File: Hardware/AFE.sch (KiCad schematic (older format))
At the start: 38 parts, among them U801 4069, U802 MCP47CXBX2

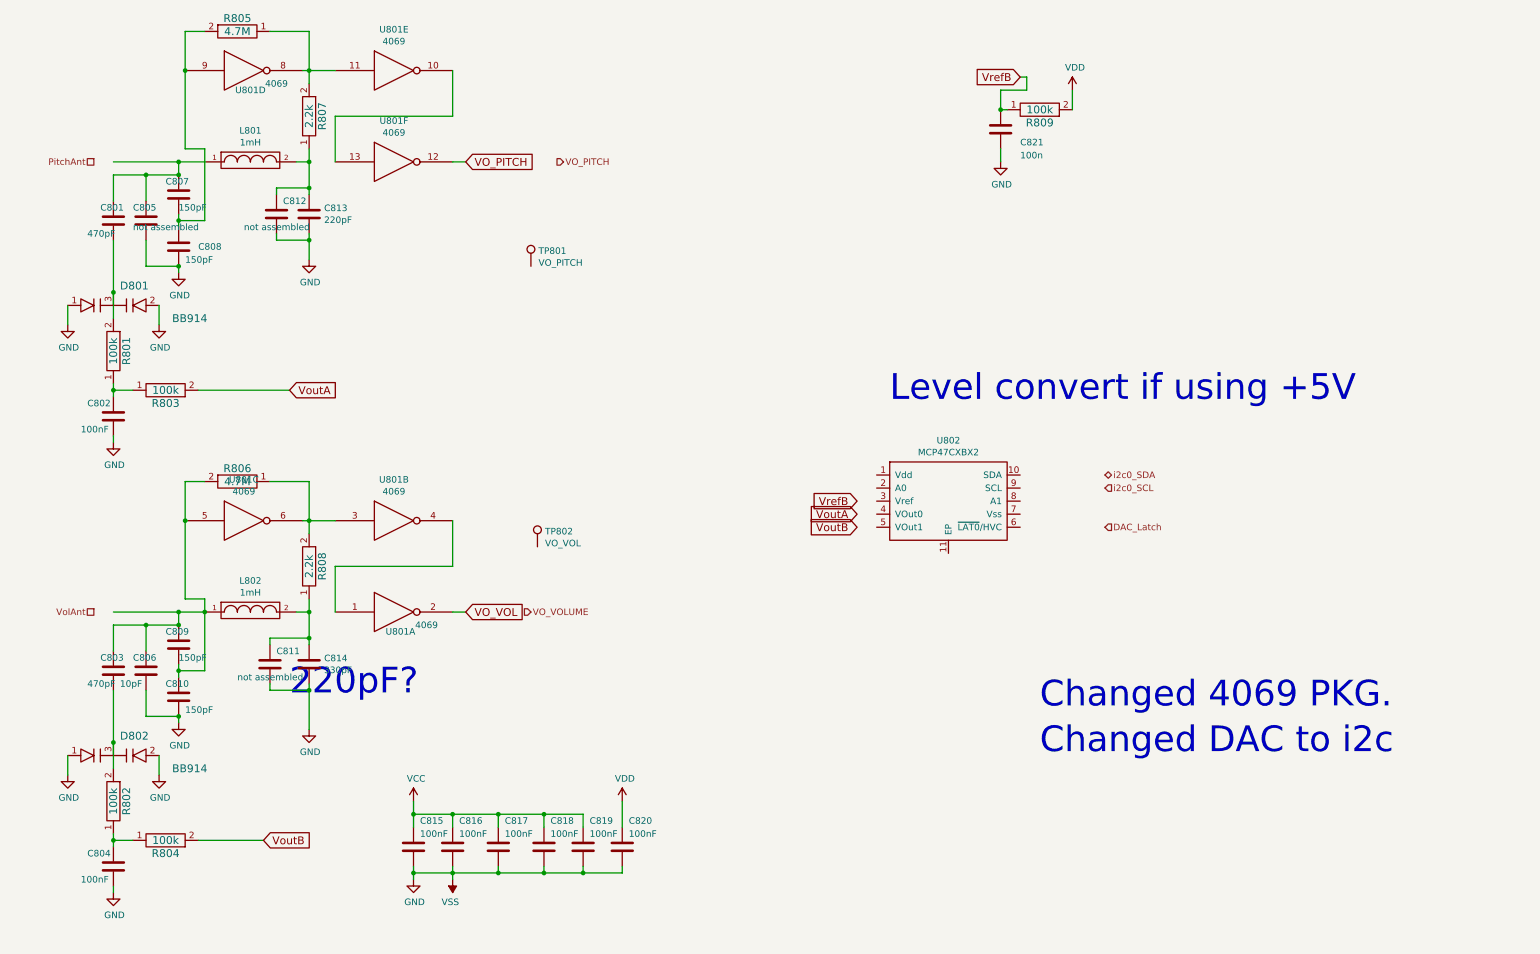
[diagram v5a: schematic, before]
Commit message: Adding power to the 4069.
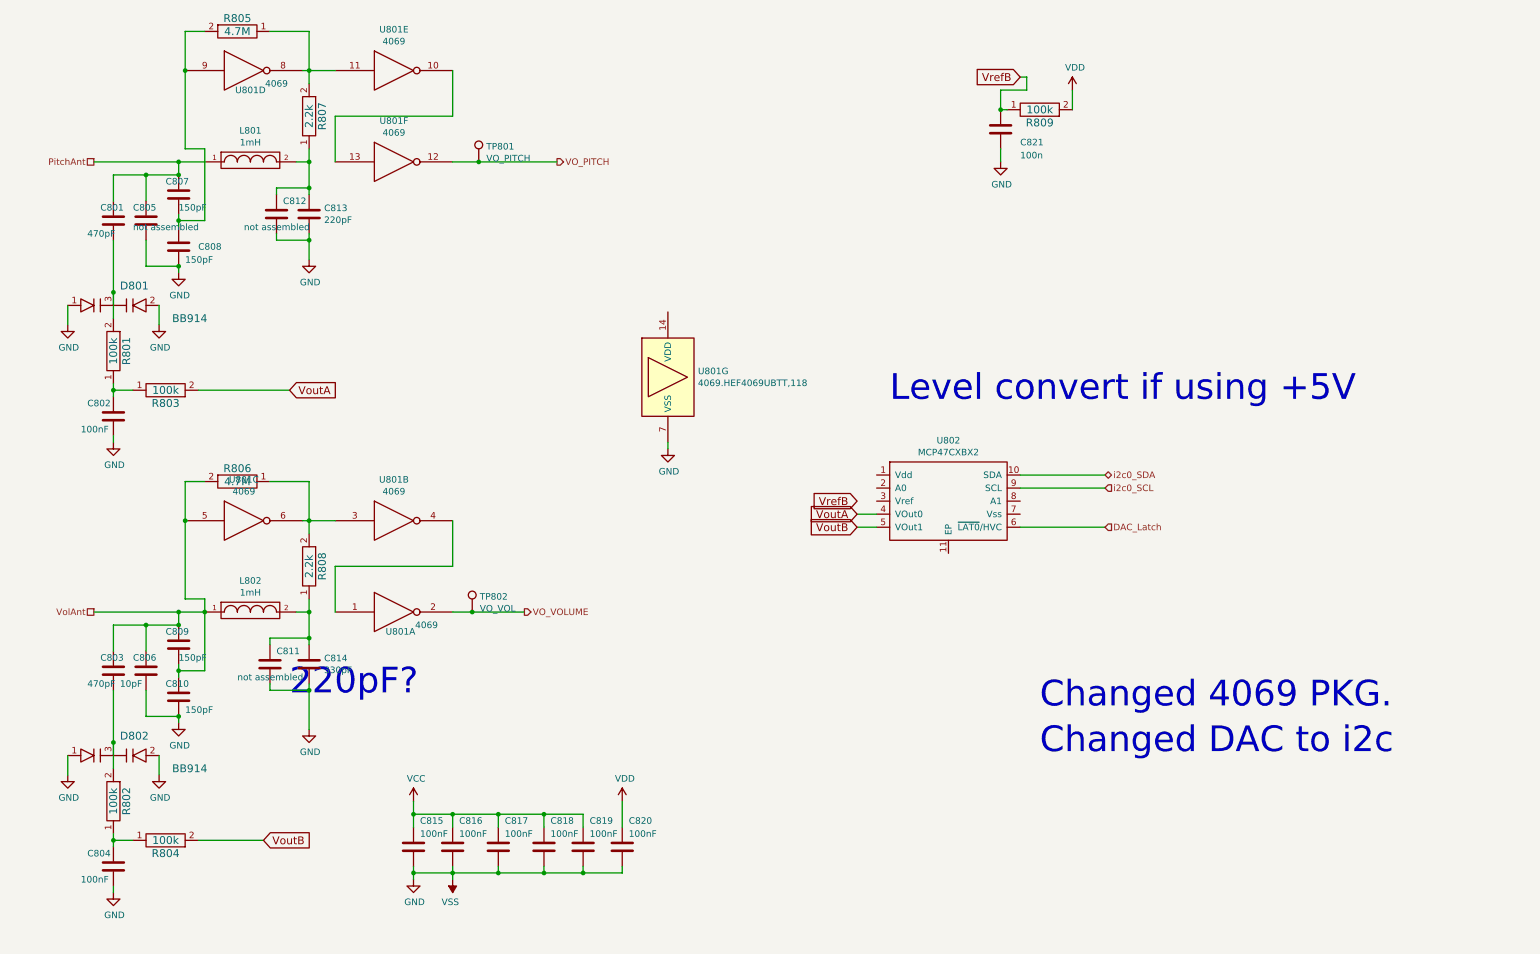
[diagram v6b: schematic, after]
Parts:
- added unit 7 of U801
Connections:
- net VO_VOL is gone; now on net VO_VOLUME: U801.2
- net DAC_Latch: now also U802.6 (~LAT0~/HVC)
- net GND: now also U801.7 (VSS)
- net PitchAnt: now also C801.1, C805.1, C807.1, L801.1
- net VDD: now also U801.14 (VDD)
- net VO_PITCH: now also TP801.1
- net VO_VOLUME: now also TP802.1
- net VolAnt: now also C803.1, C806.1, C809.1, C809.2, C810.1, L802.1, R806.2, U801.5
- net VoutA: now also U802.4 (VOut0)
- net VoutB: now also U802.5 (VOut1)
- net i2c0_SCL: now also U802.9 (SCL)
- net i2c0_SDA: now also U802.10 (SDA)
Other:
- moved on the sheet: TP801, TP802
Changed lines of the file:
@@
 Text GLabel 2200 7000 2    60   Input ~ 0
 VoutB
-Text GLabel 3750 1800 2    60   Input ~ 0
-VO_PITCH
 Wire Wire Line
 	2750 1800 2750 1450
 Wire Wire Line
 	2750 1450 3650 1450
-Wire Wire Line
-	1050 1800 1550 1800
 Connection ~ 2550 1100
 Wire Wire Line
@@
 Wire Wire Line
 	2750 4900 3650 4900
-Wire Wire Line
-	1050 5250 1550 5250
 Connection ~ 2550 4550
 Wire Wire Line
@@
 Wire Wire Line
 	2550 2350 2550 2400
-Wire Wire Line
-	3650 5250 3750 5250
 Wire Wire Line
 	1700 3550 2400 3550
@@
 Wire Wire Line
 	2550 2400 2550 2550
-Wire Wire Line
-	3650 1800 3750 1800
-Text GLabel 3750 5250 2    60   Input ~ 0
-VO_VOL
 Text Notes 8150 6350 0    197  ~ 0
 Changed DAC to i2c
@@
 L Connector:TestPoint TP801
 U 1 1 613208C5
-P 4250 2600
-F 0 "TP801" H 4308 2718 50  0000 L CNN
-F 1 "VO_PITCH" H 4308 2627 50  0000 L CNN
-F 2 "TestPoint:TestPoint_THTPad_D1.5mm_Drill0.7mm" H 4450 2600 50  0001 C CNN
-F 3 "~" H 4450 2600 50  0001 C CNN
-	1    4250 2600
+P 3850 1800
+F 0 "TP801" H 3908 1918 50  0000 L CNN
+F 1 "VO_PITCH" H 3908 1827 50  0000 L CNN
+F 2 "TestPoint:TestPoint_THTPad_D1.5mm_Drill0.7mm" H 4050 1800 50  0001 C CNN
+F 3 "~" H 4050 1800 50  0001 C CNN
+	1    3850 1800
 	1    0    0    -1
 $EndComp
@@
 L Connector:TestPoint TP802
 U 1 1 613273AC
-P 4300 4750
-F 0 "TP802" H 4358 4868 50  0000 L CNN
-F 1 "VO_VOL" H 4358 4777 50  0000 L CNN
-F 2 "TestPoint:TestPoint_THTPad_D1.5mm_Drill0.7mm" H 4500 4750 50  0001 C CNN
-F 3 "~" H 4500 4750 50  0001 C CNN
-	1    4300 4750
+P 3800 5250
+F 0 "TP802" H 3858 5368 50  0000 L CNN
+F 1 "VO_VOL" H 3858 5277 50  0000 L CNN
+F 2 "TestPoint:TestPoint_THTPad_D1.5mm_Drill0.7mm" H 4000 5250 50  0001 C CNN
+F 3 "~" H 4000 5250 50  0001 C CNN
+	1    3800 5250
 	1    0    0    -1
 $EndComp
@@
 Text Notes 8150 6000 0    197  ~ 0
 Changed 4069 PKG.
+Wire Wire Line
+	900  1800 1550 1800
+Wire Wire Line
+	900  5250 1550 5250
+Wire Wire Line
+	3650 5250 3800 5250
+Connection ~ 3800 5250
+Wire Wire Line
+	3800 5250 4200 5250
+Wire Wire Line
+	3650 1800 3850 1800
+Connection ~ 3850 1800
+Wire Wire Line
+	3850 1800 4450 1800
+Wire Wire Line
+	6750 4500 6900 4500
+Wire Wire Line
+	6750 4600 6900 4600
+Wire Wire Line
+	8000 4600 8650 4600
+Wire Wire Line
+	8650 4300 8000 4300
+Wire Wire Line
+	8000 4200 8650 4200
+$Comp
+L OHMC2022:4069.HEF4069UBTT,118 U801
+U 7 1 613095C0
+P 5300 3450
+F 0 "U801" H 5530 3496 50  0000 L CNN
+F 1 "4069.HEF4069UBTT,118" H 5530 3405 50  0000 L CNN
+F 2 "OHMC2022:TSSOP14" H 5300 3450 60  0001 C CNN
+F 3 "http://www.diodes.com/_files/datasheets/AP131.pdf" H 5300 3450 60  0001 C CNN
+F 4 "HEF4069UBTT,118" H 5300 3450 50  0001 C CNN "MPN"
+F 5 "1727-6749-1-ND" H 5300 3450 50  0001 C CNN "DPN"
+	7    5300 3450
+	1    0    0    -1
+$EndComp
+$Comp
+L power:GND #PWR0103
+U 1 1 6130B519
+P 5300 4000
+F 0 "#PWR0103" H 5300 3750 50  0001 C CNN
+F 1 "GND" H 5308 3827 50  0000 C CNN
+F 2 "" H 5300 4000 50  0000 C CNN
+F 3 "" H 5300 4000 50  0000 C CNN
+	1    5300 4000
+	1    0    0    -1
+$EndComp
+Wire Wire Line
+	5300 4000 5300 3950
 $EndSCHEMATC

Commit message: Checking in bits.
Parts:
- U801: value 4069 -> 4069.HEF4069UBTT,118
- U801: value 4069 -> 4069.HEF4069UBTT,118; DPN (none) -> 1727-6749-1-ND; MPN (none) -> HEF4069UBTT,118
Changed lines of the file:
@@
 P 3200 4550
 F 0 "U801" H 3200 4865 50  0000 C CNN
-F 1 "4069" H 3200 4774 50  0000 C CNN
+F 1 "4069.HEF4069UBTT,118" H 3200 4774 50  0000 C CNN
 F 2 "OHMC2022:TSSOP14" H 3200 4550 60  0001 C CNN
-F 3 "https://assets.nexperia.com/documents/data-sheet/HEF4069UB.pdf" H 3200 4550 60  0001 C CNN
+F 3 "http://www.diodes.com/_files/datasheets/AP131.pdf" H 3200 4550 60  0001 C CNN
 	2    3200 4550
 	1    0    0    -1
@@
 P 2050 4550
 F 0 "U801" H 2050 4865 50  0000 C CNN
-F 1 "4069" H 2050 4774 50  0000 C CNN
+F 1 "4069.HEF4069UBTT,118" H 2050 4774 50  0000 C CNN
 F 2 "OHMC2022:TSSOP14" H 2050 4550 60  0001 C CNN
-F 3 "https://assets.nexperia.com/documents/data-sheet/HEF4069UB.pdf" H 2050 4550 60  0001 C CNN
+F 3 "http://www.diodes.com/_files/datasheets/AP131.pdf" H 2050 4550 60  0001 C CNN
+F 4 "1727-6749-1-ND" H 2050 4550 50  0001 C CNN "DPN"
+F 5 "HEF4069UBTT,118" H 2050 4550 50  0001 C CNN "MPN"
 	3    2050 4550
 	1    0    0    -1
@@
 P 3200 5250
 F 0 "U801" H 3250 5100 50  0000 C CNN
-F 1 "4069" H 3450 5150 50  0000 C CNN
+F 1 "4069.HEF4069UBTT,118" H 3450 5150 50  0000 C CNN
 F 2 "OHMC2022:TSSOP14" H 3200 5250 60  0001 C CNN
-F 3 "https://assets.nexperia.com/documents/data-sheet/HEF4069UB.pdf" H 3200 5250 60  0001 C CNN
+F 3 "http://www.diodes.com/_files/datasheets/AP131.pdf" H 3200 5250 60  0001 C CNN
 F 4 "1727-6749-1-ND" H 3200 5250 50  0001 C CNN "DPN"
 F 5 "HEF4069UBTT,118" H 3200 5250 50  0001 C CNN "MPN"
@@
 P 3200 1100
 F 0 "U801" H 3200 1415 50  0000 C CNN
-F 1 "4069" H 3200 1324 50  0000 C CNN
+F 1 "4069.HEF4069UBTT,118" H 3200 1324 50  0000 C CNN
 F 2 "OHMC2022:TSSOP14" H 3200 1100 60  0001 C CNN
-F 3 "https://assets.nexperia.com/documents/data-sheet/HEF4069UB.pdf" H 3200 1100 60  0001 C CNN
+F 3 "http://www.diodes.com/_files/datasheets/AP131.pdf" H 3200 1100 60  0001 C CNN
 	5    3200 1100
 	1    0    0    -1
@@
 P 3200 1800
 F 0 "U801" H 3200 2115 50  0000 C CNN
-F 1 "4069" H 3200 2024 50  0000 C CNN
+F 1 "4069.HEF4069UBTT,118" H 3200 2024 50  0000 C CNN
 F 2 "OHMC2022:TSSOP14" H 3200 1800 60  0001 C CNN
-F 3 "https://assets.nexperia.com/documents/data-sheet/HEF4069UB.pdf" H 3200 1800 60  0001 C CNN
+F 3 "http://www.diodes.com/_files/datasheets/AP131.pdf" H 3200 1800 60  0001 C CNN
 	6    3200 1800
 	1    0    0    -1
@@
 P 2050 1100
 F 0 "U801" H 2100 950 50  0000 C CNN
-F 1 "4069" H 2300 1000 50  0000 C CNN
+F 1 "4069.HEF4069UBTT,118" H 2300 1000 50  0000 C CNN
 F 2 "OHMC2022:TSSOP14" H 2050 1100 60  0001 C CNN
-F 3 "https://assets.nexperia.com/documents/data-sheet/HEF4069UB.pdf" H 2050 1100 60  0001 C CNN
+F 3 "http://www.diodes.com/_files/datasheets/AP131.pdf" H 2050 1100 60  0001 C CNN
 	4    2050 1100
 	1    0    0    -1
